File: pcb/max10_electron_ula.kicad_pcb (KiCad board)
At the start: 4 copper layers, 55 x 89 mm, 85 parts

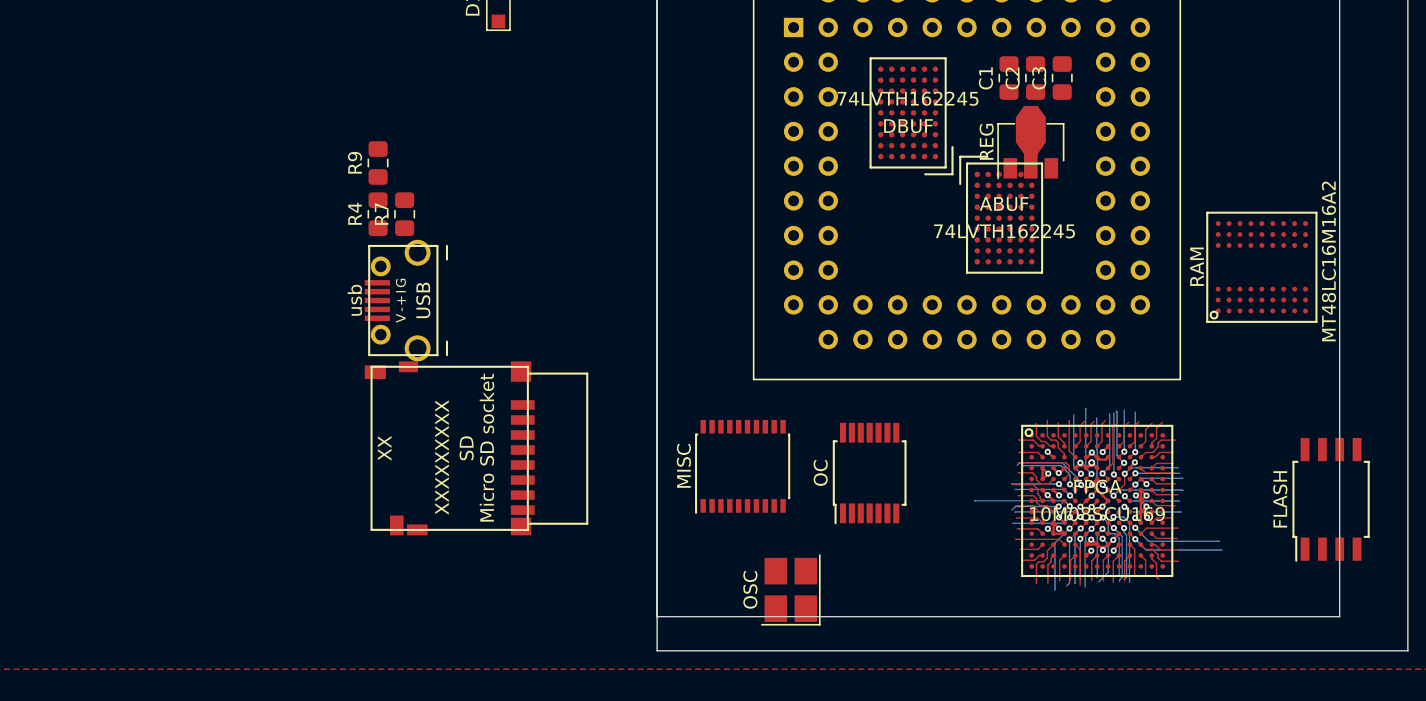
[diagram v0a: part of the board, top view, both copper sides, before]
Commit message: Added all signals to FPGA -- pins not properly assigned yet; just to make sure they'll fit at all.
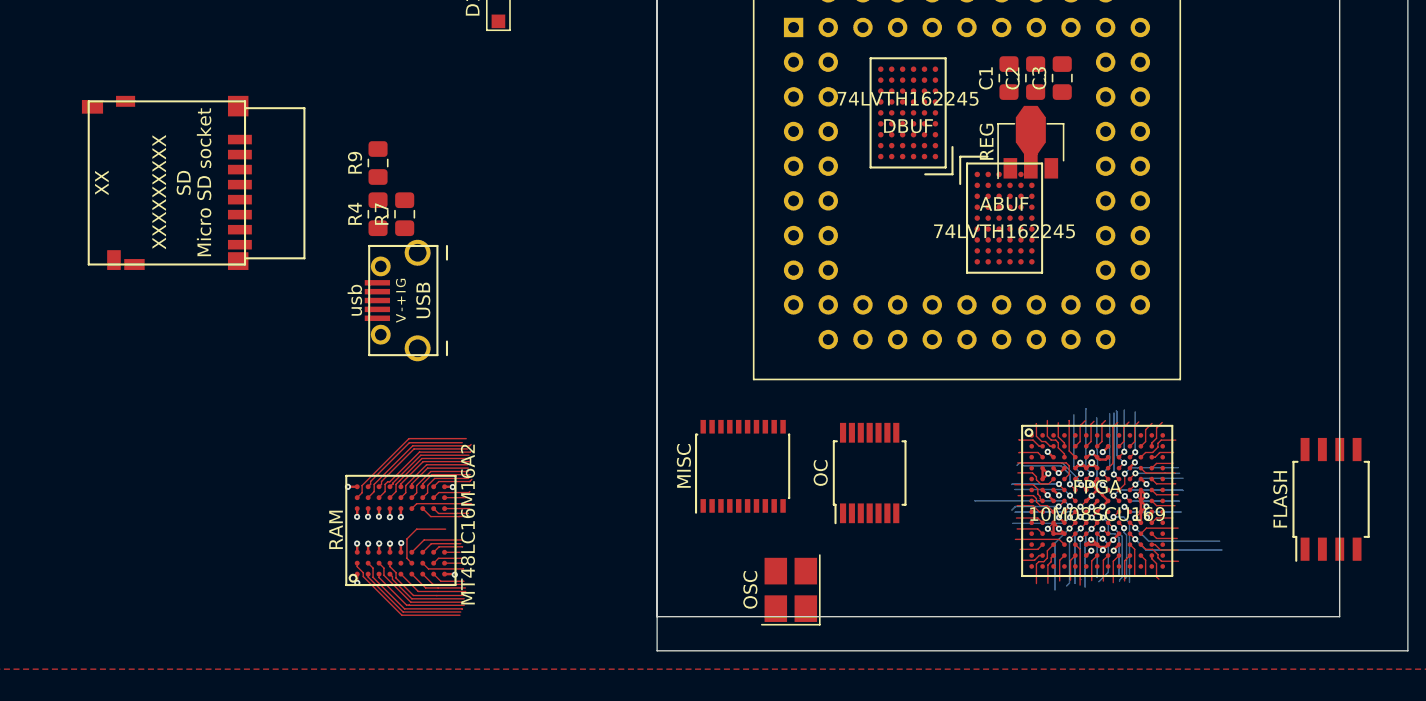
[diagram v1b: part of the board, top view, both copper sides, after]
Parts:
- moved RAM 65.9 mm to (128.5, 97.6)
- moved SD 28.4 mm to (105.6, 72.2)
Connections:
- net conn113 renamed nROMCS
- net conn114 renamed fpga_dummy0
- net conn115 renamed fpga_dummy1
- net conn116 renamed fpga_dummy2
- net conn117 renamed fpga_dummy3
- net conn49 renamed sd_DAT2
- net conn80 renamed D0
- net conn81 renamed D1
- net conn82 renamed D2
- net conn83 renamed D3
- net conn84 renamed D4
- net conn85 renamed D5
- net conn86 renamed D6
- net conn87 renamed D7
- FPGA pad A10: conn8 -> sdram_DQ2
- FPGA pad A11: conn9 -> sdram_DQ3
- FPGA pad A12: conn10 -> sdram_DQ4
- FPGA pad A2: conn0 -> flash_nCE
- FPGA pad A3: conn1 -> flash_SCK
- FPGA pad A4: conn2 -> flash_IO0
- FPGA pad A5: conn3 -> flash_IO1
- FPGA pad A6: conn4 -> flash_IO2
- FPGA pad A7: conn5 -> flash_IO3
- FPGA pad A8: conn6 -> sdram_DQ0
- FPGA pad A9: conn7 -> sdram_DQ1
- FPGA pad B1: conn20 -> sdram_DQ14
- FPGA pad B10: conn44 -> sdram_LDQM
- FPGA pad B11: conn45 -> sd_CLK_SCK
- FPGA pad B12: conn64 -> A2
- FPGA pad B13: conn29 -> sdram_A7
- FPGA pad B2: conn38 -> sdram_nWE
- FPGA pad B3: conn39 -> sdram_nCAS
- FPGA pad B4: conn40 -> sdram_nRAS
- FPGA pad B5: conn41 -> sdram_CLK
- FPGA pad B6: conn42 -> sdram_CKE
- FPGA pad B7: conn43 -> sdram_UDQM
- FPGA pad C1: conn21 -> sdram_DQ15
- FPGA pad C10: conn63 -> A1
- FPGA pad C11: conn77 -> A15
- FPGA pad C12: conn65 -> A3
- FPGA pad C13: conn30 -> sdram_A8
- FPGA pad C2: conn56 -> dac_lrclk
- FPGA pad C9: conn62 -> A0
- FPGA pad D1: conn22 -> sdram_A0
- FPGA pad D11: conn66 -> A4
- FPGA pad D12: conn67 -> A5
- FPGA pad D13: conn31 -> sdram_A9
- FPGA pad E1: conn23 -> sdram_A1
- FPGA pad E12: conn68 -> A6
- FPGA pad E13: conn111 -> CAS_OUT
- FPGA pad E3: conn78 -> D_buf_nOE
- FPGA pad E9: conn95 -> RnW_in
- FPGA pad F1: conn24 -> sdram_A2
- FPGA pad F12: conn69 -> A7
- FPGA pad F13: conn112 -> CAS_IN
- FPGA pad F4: conn96 -> CLK_16MHZ
- FPGA pad G10: conn109 -> nCSYNC
- FPGA pad G12: conn70 -> A8
- FPGA pad G13: conn32 -> sdram_A10
- FPGA pad G5: conn105 -> nHS
- FPGA pad G9: conn110 -> CAS_MO
- FPGA pad H1: conn25 -> sdram_A3
- FPGA pad H10: conn98 -> nRESET_out
- FPGA pad H13: conn33 -> sdram_A11
- FPGA pad H2: conn57 -> dac_bclk
- FPGA pad H3: conn104 -> PHI_OUT
- FPGA pad H4: conn108 -> BLUE
- FPGA pad H5: conn107 -> GREEN
- FPGA pad H6: conn106 -> RED
- FPGA pad H9: conn97 -> CAPS_LOCK
- FPGA pad J1: conn26 -> sdram_A4
- FPGA pad J10: conn90 -> KBD1
- FPGA pad J12: conn71 -> A9
- FPGA pad J13: conn34 -> sdram_A12
- FPGA pad J2: conn58 -> dac_mclk
- FPGA pad J5: conn88 -> input_buf_nOE
- FPGA pad J6: conn89 -> KBD0
- FPGA pad J7: conn99 -> nIRQ_out
- FPGA pad J8: conn100 -> RnW_out
- FPGA pad J9: conn101 -> RnW_nOE
- FPGA pad K1: conn27 -> sdram_A5
- FPGA pad K10: conn93 -> nNMI_in
- FPGA pad K11: conn72 -> A10
- FPGA pad K12: conn73 -> A11
- FPGA pad K13: conn35 -> sdram_BA0
- FPGA pad K2: conn59 -> dac_nmute
- FPGA pad K5: conn102 -> nRESET_in
- FPGA pad K6: conn103 -> misc_buf_nOE
- FPGA pad K7: conn91 -> KBD2
- FPGA pad K8: conn92 -> KBD3
- FPGA pad L10: conn76 -> A14
- FPGA pad L11: conn74 -> A12
- FPGA pad L12: conn75 -> A13
- FPGA pad L13: conn36 -> sdram_BA1
- FPGA pad L2: conn60 -> A_buf_nOE
- FPGA pad L3: conn61 -> A_buf_DIR
- FPGA pad L4: conn94 -> nIRQ_in
- FPGA pad L5: conn79 -> D_buf_DIR
- FPGA pad M1: conn28 -> sdram_A6
- FPGA pad M10: conn53 -> USB_PU
- FPGA pad M11: conn54 -> clock_osc
- FPGA pad M12: conn55 -> dac_dacdat
- FPGA pad M13: conn37 -> sdram_nCS
- FPGA pad M2: conn46 -> sd_CMD_MOSI
- FPGA pad M3: conn47 -> sd_DAT0_MISO
- FPGA pad M4: conn48 -> sd_DAT1
- FPGA pad M7: conn40 -> sdram_nRAS
- FPGA pad M8: conn51 -> USB_M
- FPGA pad M9: conn52 -> USB_P
- FPGA pad N10: conn17 -> sdram_DQ11
- FPGA pad N11: conn18 -> sdram_DQ12
- FPGA pad N12: conn19 -> sdram_DQ13
- FPGA pad N4: conn11 -> sdram_DQ5
- FPGA pad N5: conn12 -> sdram_DQ6
- FPGA pad N6: conn13 -> sdram_DQ7
- FPGA pad N7: conn14 -> sdram_DQ8
- FPGA pad N8: conn15 -> sdram_DQ9
- FPGA pad N9: conn16 -> sdram_DQ10
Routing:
- net sdram_DQ0: track 0.00 -> 10.1 mm
- net sdram_DQ2: track 0.00 -> 9.47 mm
- net sdram_DQ15: track 0.00 -> 9.42 mm
- net sdram_nRAS: track 0.00 -> 9.15 mm
- net sdram_DQ13: track 0.00 -> 8.69 mm
- net sdram_DQ4: track 0.00 -> 8.43 mm
- net sdram_DQ1: track 0.00 -> 8.35 mm
- net sdram_LDQM: track 0.00 -> 8.26 mm
- net sdram_DQ14: track 0.00 -> 8.06 mm
- net sdram_DQ3: track 0.00 -> 7.74 mm
- net sdram_DQ11: track 0.00 -> 7.73 mm
- net conn108: track 7.70 -> 0.00 mm, vias 1 -> 0
- net BLUE: track 0.00 -> 7.70 mm, vias 0 -> 1
- net sdram_DQ12: track 0.00 -> 7.33 mm
- net sdram_DQ6: track 0.00 -> 7.29 mm
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
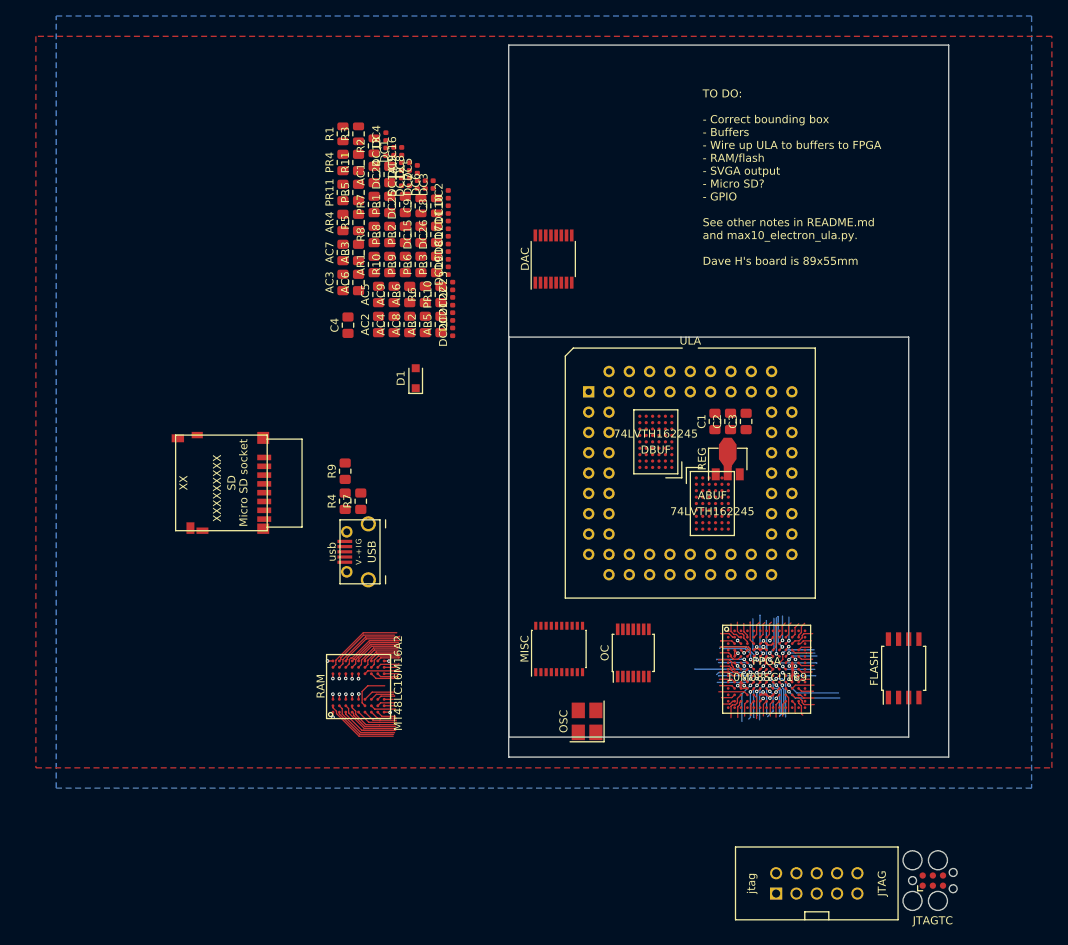
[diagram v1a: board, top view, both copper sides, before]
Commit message: Making progress wiring up all the signals inside the ULA socket
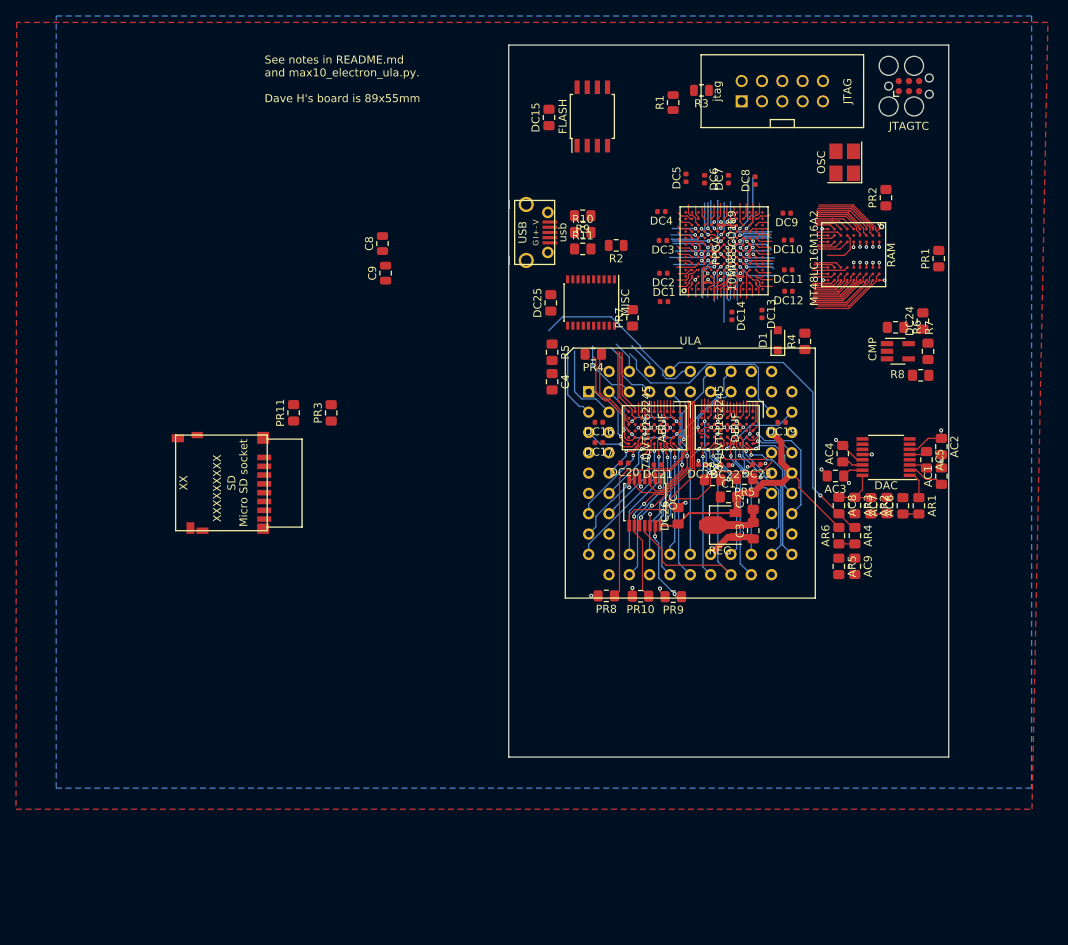
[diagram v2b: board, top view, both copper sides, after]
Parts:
- added CMP: MIC7221, Package_TO_SOT_SMD:SOT-23-5_HandSoldering, F.Cu at (195.9, 55.7)
- moved JTAGTC 99.4 mm to (197.3, 22.6)
- moved JTAG 99.1 mm to (181.4, 23.2)
- moved RAM 82.1 mm to (190.3, 43.6), turned to 270 degrees
- moved AC1 80.3 mm to (201.3, 71.3)
- moved FLASH 79.2 mm to (157.7, 26.4)
- moved OSC 76.9 mm to (189.2, 32.1)
- moved AR4 75.0 mm to (190.5, 78.8), turned to 270 degrees
- moved AC7 75.0 mm to (194.5, 75.0)
- moved AR1 74.5 mm to (198.5, 75.0), turned to 270 degrees
- moved AC6 73.5 mm to (196.5, 75.0)
- moved R7 73.3 mm to (199.6, 55.7), turned to 270 degrees
- moved AC2 72.0 mm to (201.3, 67.6), turned to 270 degrees
- moved AC5 71.5 mm to (199.4, 69.3), turned to 270 degrees
- moved R8 70.6 mm to (198.7, 58.7), turned to 180 degrees
- moved AR3 69.6 mm to (190.5, 75.0), turned to 270 degrees
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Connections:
- net D0 renamed io_b6_R31n_D9
- net D1 renamed io_b1A_L3p_E4
- net D2 renamed io_b8_T22p_E6
- net D3 renamed io_b8_T18n_E8
- net D4 renamed io_b6_R31p_E10
- net D5 renamed io_b6_R27p_F8
- net D6 renamed io_b1B_L14p_G4
- net D7 renamed io_b5_R10n_H8
- net PD0 renamed data7
- net PD1 renamed data4
- net PD2 renamed data5
- net PD3 renamed data1
- net PD4 renamed data2
- net PD5 renamed data3
- net PD6 renamed data6
- net PD7 renamed data0
- net fpga_dummy0 renamed special_b2_DPCLK1_L22p_N3
- net fpga_dummy1 renamed special_b6_DPCLK2_R26n_F10
- net fpga_dummy2 renamed special_b6_DPCLK3_R26p_F9
- net fpga_dummy3 renamed special_VREFB2N0_nodiff_L1
- net nROM renamed ROM_n
- net nROMCS renamed special_b2_DPCLK0_L22n_N2
- net sd_DAT2 renamed io_b3_B2p_M5
- ABUF pad A1: A0 -> addr15
- ABUF pad A6: A0_5V -> A15_5V
- ABUF pad B1: A2 -> addr9
- ABUF pad B2: A1 -> addr10
- ABUF pad B5: A1_5V -> A10_5V
- ABUF pad B6: A2_5V -> A9_5V
- ABUF pad C1: A4 -> addr3
- ABUF pad C2: A3 -> addr11
- ABUF pad C5: A3_5V -> A11_5V
- ABUF pad C6: A4_5V -> A3_5V
- ABUF pad D1: A6 -> addr5
- ABUF pad D2: A5 -> addr4
- ABUF pad D5: A5_5V -> A4_5V
- ABUF pad D6: A6_5V -> A5_5V
- ABUF pad E1: A8 -> addr6
- ABUF pad E2: A7 -> addr13
- ABUF pad E5: A7_5V -> A13_5V
- ABUF pad E6: A8_5V -> A6_5V
- ABUF pad F1: A10 -> addr7
- ABUF pad F2: A9 -> addr2
- ABUF pad F5: A9_5V -> A2_5V
- ABUF pad F6: A10_5V -> A7_5V
- ABUF pad G1: A12 -> addr12
- ABUF pad G2: A11 -> addr14
- ABUF pad G5: A11_5V -> A14_5V
- ABUF pad H1: A14 -> addr0
- ABUF pad H2: A13 -> addr8
- ABUF pad H5: A13_5V -> A8_5V
- ABUF pad H6: A14_5V -> A0_5V
- ABUF pad J1: A15 -> addr1
- ABUF pad J6: A15_5V -> A1_5V
- AC8 pad 1: dac_out_left -> dac_out_right
- AR3 pad 1: dac_out_left -> dac_out_right
- D1 pad 2: nRESET_in -> RST_n_in
- DBUF pad A6: PD0_5V -> PD7_5V
- DBUF pad B5: PD1_5V -> PD4_5V
- DBUF pad B6: PD2_5V -> PD5_5V
- DBUF pad C5: PD3_5V -> PD1_5V
- DBUF pad C6: PD4_5V -> PD2_5V
- DBUF pad D5: PD5_5V -> PD3_5V
- DBUF pad E1: KBD0 -> clk_in
- DBUF pad E5: PD7_5V -> PD0_5V
- DBUF pad E6: KBD0_5V -> clk_in_5V
- DBUF pad F1: KBD2 -> kbd3
- DBUF pad F2: KBD1 -> RnW_in
- DBUF pad F5: KBD1_5V -> RnW_5V
- DBUF pad F6: KBD2_5V -> KBD3_5V
- DBUF pad G1: nNMI_in -> IRQ_n_in
- DBUF pad G2: KBD3 -> kbd2
- DBUF pad G5: KBD3_5V -> KBD2_5V
- DBUF pad G6: nNMI_5V -> nIRQ_5V
- DBUF pad H1: RnW_in -> kbd1
- DBUF pad H2: nIRQ_in -> NMI_n_in
- DBUF pad H5: nIRQ_5V -> nNMI_5V
- DBUF pad H6: RnW_5V -> KBD1_5V
- DBUF pad J1: CLK_16MHZ -> kbd0
- DBUF pad J6: CLK_16MHZ_5V -> KBD0_5V
- DC26 pad 1: 3V3 -> 5V
- FPGA pad A10: sdram_DQ2 -> io_b8_T17p_A10
- FPGA pad A11: sdram_DQ3 -> io_b8_T17n_A11
- FPGA pad A12: sdram_DQ4 -> io_b6_R30n_A12
- FPGA pad A2: flash_nCE -> io_b8_T26p_A2
- FPGA pad A3: flash_SCK -> io_b8_T21n_A3
- FPGA pad A4: flash_IO0 -> io_b8_T21p_A4
- FPGA pad A5: flash_IO1 -> TODO_unknown_b8_A5
- FPGA pad A6: flash_IO2 -> io_b8_T19n_A6
- FPGA pad A7: flash_IO3 -> io_b8_T19p_A7
- FPGA pad A8: sdram_DQ0 -> io_b8_T15p_A8
- FPGA pad A9: sdram_DQ1 -> io_b8_T15n_A9
- FPGA pad B1: sdram_DQ14 -> io_b1A_L5p_B1
- FPGA pad B10: sdram_LDQM -> io_b8_T16p_B10
- FPGA pad B11: sd_CLK_SCK -> io_b6_R28n_B11
- FPGA pad B12: A2 -> io_b6_R28p_B12
- FPGA pad B13: sdram_A7 -> io_b6_R30p_B13
- FPGA pad B2: sdram_nWE -> io_b8_T26n_B2
- FPGA pad B3: sdram_nCAS -> io_b8_T23p_B3
- FPGA pad B4: sdram_nRAS -> io_b8_T23n_B4
- FPGA pad B5: sdram_CLK -> io_b8_T20n_B5
- FPGA pad B6: sdram_CKE -> io_b8_T20p_B6
- FPGA pad B7: sdram_UDQM -> special_VREFB8N0_nodiff_B7
- FPGA pad C1: sdram_DQ15 -> io_b1A_L5n_C1
- FPGA pad C10: A1 -> io_b8_T14p_C10
- FPGA pad C11: A15 -> io_b6_R29n_C11
- FPGA pad C12: A3 -> io_b6_R29p_C12
- FPGA pad C13: sdram_A8 -> TODO_unknown_b6_C13
- FPGA pad C2: dac_lrclk -> io_b1A_L1p_C2
- FPGA pad C9: A0 -> io_b8_T14n_C9
- FPGA pad D1: sdram_A0 -> io_b1A_L1n_D1
- FPGA pad D11: A4 -> io_b6_R33n_D11
- FPGA pad D12: A5 -> io_b6_R33p_D12
- FPGA pad D13: sdram_A9 -> special_VREFB6N0_nodiff_D13
- FPGA pad D6: GND -> fpga_CRC_ERROR
- FPGA pad D7: GND -> fpga_CONFIG_SEL
- FPGA pad E1: sdram_A1 -> io_b1A_L7p_E1
- FPGA pad E12: A6 -> io_b6_R18n_E12
- FPGA pad E13: CAS_OUT -> special_b6_CLK3n_R16n_E13
- FPGA pad E3: D_buf_nOE -> io_b1A_L3n_E3
- FPGA pad E7: 3V3 -> fpga_nCONFIG
- FPGA pad E9: RnW_in -> io_b6_R27n_E9
- FPGA pad F1: sdram_A2 -> io_b1A_L7n_F1
- FPGA pad F12: A7 -> io_b6_R18p_F12
- FPGA pad F13: CAS_IN -> special_b6_CLK3p_R16p_F13
- FPGA pad F4: CLK_16MHZ -> io_b1B_L14n_F4
- FPGA pad G10: nCSYNC -> special_b6_CLK2n_R14n_G10
- FPGA pad G12: A8 -> io_b5_R11n_G12
- FPGA pad G13: sdram_A10 -> io_b5_R11p_G13
- FPGA pad G5: nHS -> special_b2_CLK0n_L18n_G5
- FPGA pad G9: CAS_MO -> special_b6_CLK2p_R14p_G9
- FPGA pad H1: sdram_A3 -> special_VREFB1N0_nodiff_H1
- FPGA pad H10: nRESET_out -> io_b5_R8n_H10
- FPGA pad H13: sdram_A11 -> io_b5_R9n_H13
- FPGA pad H2: dac_bclk -> io_b1B_L16n_H2
- FPGA pad H3: PHI_OUT -> io_b1B_L16p_H3
- FPGA pad H4: BLUE -> special_b2_CLK1p_L20p_H4
- FPGA pad H5: GREEN -> special_b2_CLK1n_L20n_H5
- FPGA pad H6: RED -> special_b2_CLK0p_L18p_H6
- FPGA pad H9: CAPS_LOCK -> io_b5_R10p_H9
- FPGA pad J1: sdram_A4 -> io_b2_L19n_J1
- FPGA pad J10: KBD1 -> io_b5_R1n_J10
- FPGA pad J12: A9 -> io_b5_R7n_J12
- FPGA pad J13: sdram_A12 -> io_b5_R9p_J13
- FPGA pad J2: dac_mclk -> io_b2_L19p_J2
- FPGA pad J5: input_buf_nOE -> io_b3_B3p_J5
- FPGA pad J6: KBD0 -> io_b3_B7n_J6
- FPGA pad J7: nIRQ_out -> io_b3_B9n_J7
- FPGA pad J8: RnW_out -> io_b3_B14n_J8
- FPGA pad J9: RnW_nOE -> io_b5_R8p_J9
- FPGA pad K1: sdram_A5 -> io_b2_L28n_K1
- FPGA pad K10: nNMI_in -> io_b5_R1p_K10
- FPGA pad K11: A10 -> io_b5_R2p_K11
- FPGA pad K12: A11 -> io_b5_R7p_K12
- FPGA pad K13: sdram_BA0 -> special_VREFB5N0_nodiff_K13
- FPGA pad K2: dac_nmute -> io_b2_L28p_K2
- FPGA pad K5: nRESET_in -> io_b3_B3n_K5
- FPGA pad K6: misc_buf_nOE -> io_b3_B7p_K6
- FPGA pad K7: KBD2 -> io_b3_B9p_K7
- FPGA pad K8: KBD3 -> io_b3_B14p_K8
- FPGA pad L10: A14 -> io_b3_B16p_L10
- FPGA pad L11: A12 -> io_b3_B12p_L11
- FPGA pad L12: A13 -> io_b5_R2n_L12
- FPGA pad L13: sdram_BA1 -> TODO_unknown_b5_L13
- FPGA pad L2: A_buf_nOE -> TODO_unknown_b2_L2
- FPGA pad L3: A_buf_DIR -> special_b2_PLL_L_CLKOUTp_L27p_L3
- FPGA pad L4: nIRQ_in -> io_b3_B1p_L4
- FPGA pad L5: D_buf_DIR -> io_b3_B1n_L5
- FPGA pad M1: sdram_A6 -> io_b2_L21n_M1
- FPGA pad M10: USB_PU -> io_b3_B16n_M10
- FPGA pad M11: clock_osc -> io_b3_B12n_M11
- FPGA pad M12: dac_dacdat -> io_b3_B10p_M12
- FPGA pad M13: sdram_nCS -> io_b3_B10n_M13
- FPGA pad M2: sd_CMD_MOSI -> io_b2_L21p_M2
- FPGA pad M3: sd_DAT0_MISO -> special_b2_PLL_L_CLKOUTn_L27n_M3
- FPGA pad M4: sd_DAT1 -> io_b3_B2n_M4
- FPGA pad M7: sdram_nRAS -> io_b3_B5p_M7
- FPGA pad M8: USB_M -> io_b3_B8n_M8
- FPGA pad M9: USB_P -> io_b3_B8p_M9
- FPGA pad N10: sdram_DQ11 -> io_b3_B11n_N10
- FPGA pad N11: sdram_DQ12 -> special_VREFB3N0_nodiff_N11
- FPGA pad N12: sdram_DQ13 -> TODO_unknown_b3_N12
- FPGA pad N4: sdram_DQ5 -> io_b3_B4n_N4
- FPGA pad N5: sdram_DQ6 -> io_b3_B4p_N5
- FPGA pad N6: sdram_DQ7 -> io_b3_B5n_N6
- FPGA pad N7: sdram_DQ8 -> io_b3_B6n_N7
- FPGA pad N8: sdram_DQ9 -> io_b3_B6p_N8
- FPGA pad N9: sdram_DQ10 -> io_b3_B11p_N9
- MISC pad 11: CAS_OUT_5V -> PHI_OUT_5V_prefilter
- MISC pad 12: CAS_MO_5V -> nHS_5V
- MISC pad 13: nCSYNC_5V -> red_5V
- MISC pad 14: BLUE_5V -> green_5V
- MISC pad 15: GREEN_5V -> blue_5V
- MISC pad 16: RED_5V -> csync_5V
- MISC pad 17: nHS_5V -> CAS_MO_5V
- MISC pad 18: PHI_OUT_5V_prefilter -> CAS_OUT_5V
- MISC pad 2: PHI_OUT -> casOut
- MISC pad 3: nHS -> casMO
- MISC pad 4: RED -> csync
- MISC pad 5: GREEN -> blue
- MISC pad 6: BLUE -> green
- MISC pad 7: nCSYNC -> red
- MISC pad 8: CAS_MO -> HS_n
- MISC pad 9: CAS_OUT -> clk_out
- OC pad 10: nIRQ_out -> RnW_out
- OC pad 11: RnW_5V -> nIRQ_5V
- OC pad 12: RnW_nOE -> GND
- OC pad 13: RnW_out -> IRQ_n_out
- OC pad 2: CAPS_LOCK -> caps
- OC pad 4: nRESET_out -> RST_n_out
- OC pad 8: nIRQ_5V -> RnW_5V
- OC pad 9: GND -> RnW_nOE
- OSC pad 3: clock_osc -> clk_osc
- PR8 pad 1: nRESET_out -> RST_n_out
- PR9 pad 1: nIRQ_out -> IRQ_n_out
- R4 pad 2: nRESET_in -> RST_n_in
- R6 pad 1: CAS_IN -> casIn
- ULA pad 3: RED_5V -> red_5V
- ULA pad 4: GREEN_5V -> green_5V
- ULA pad 49: CLK_16MHZ_5V -> clk_in_5V
- ULA pad 65: nCSYNC_5V -> csync_5V
- ULA pad 66: BLUE_5V -> blue_5V
- ULA pad 9: 5V -> (no net)
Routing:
- net SOUND_OUT_5V: track 0.00 -> 39.1 mm, vias 0 -> 1
- net 5V: track 0.00 -> 35.6 mm
- net 3V3: track 32.5 -> 66.9 mm, vias 25 -> 43
- net RnW_5V: track 0.00 -> 33.0 mm, vias 0 -> 1
- net nIRQ_5V: track 0.00 -> 32.6 mm, vias 0 -> 1
- net GND: track 15.9 -> 48.4 mm, vias 19 -> 42
- net RST_n_out: track 0.00 -> 32.2 mm
- net IRQ_n_out: track 0.00 -> 29.6 mm, vias 0 -> 3
- net CAS_OUT_5V: track 0.00 -> 25.6 mm
- net RnW_nOE: track 4.47 -> 28.4 mm, vias 1 -> 2
- net nRESET_5V: track 0.00 -> 23.0 mm, vias 0 -> 1
- net PHI_OUT_5V: track 0.00 -> 22.5 mm
- net PD1_5V: track 0.00 -> 18.6 mm, vias 0 -> 1
- net A5_5V: track 0.00 -> 18.3 mm, vias 0 -> 1
- net KBD3_5V: track 0.00 -> 18.3 mm, vias 0 -> 1
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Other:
- outline, holes or cut-outs redrawn
- board text added: "See notes in README.md and max10_electron_ula.py. Dave H's board is 89x55mm"
- board text removed: "TO DO: - Correct bounding box - Buffers - Wire up ULA to buffers to FPGA - RAM/flash - SVGA output - Micro SD? - GPIO See other notes in README.md and max10_electron_ula.py. Dave H's board is 89x55mm"
